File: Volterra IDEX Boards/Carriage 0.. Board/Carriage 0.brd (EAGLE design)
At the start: 84.5 x 61.3 mm, 20 parts, among them K1 FFC/FPC/34PIN/1MMPITCH/TOPLOCK, K2 Tool 0, X1 EXTDR-0, X4 24V, X5 X_LMT

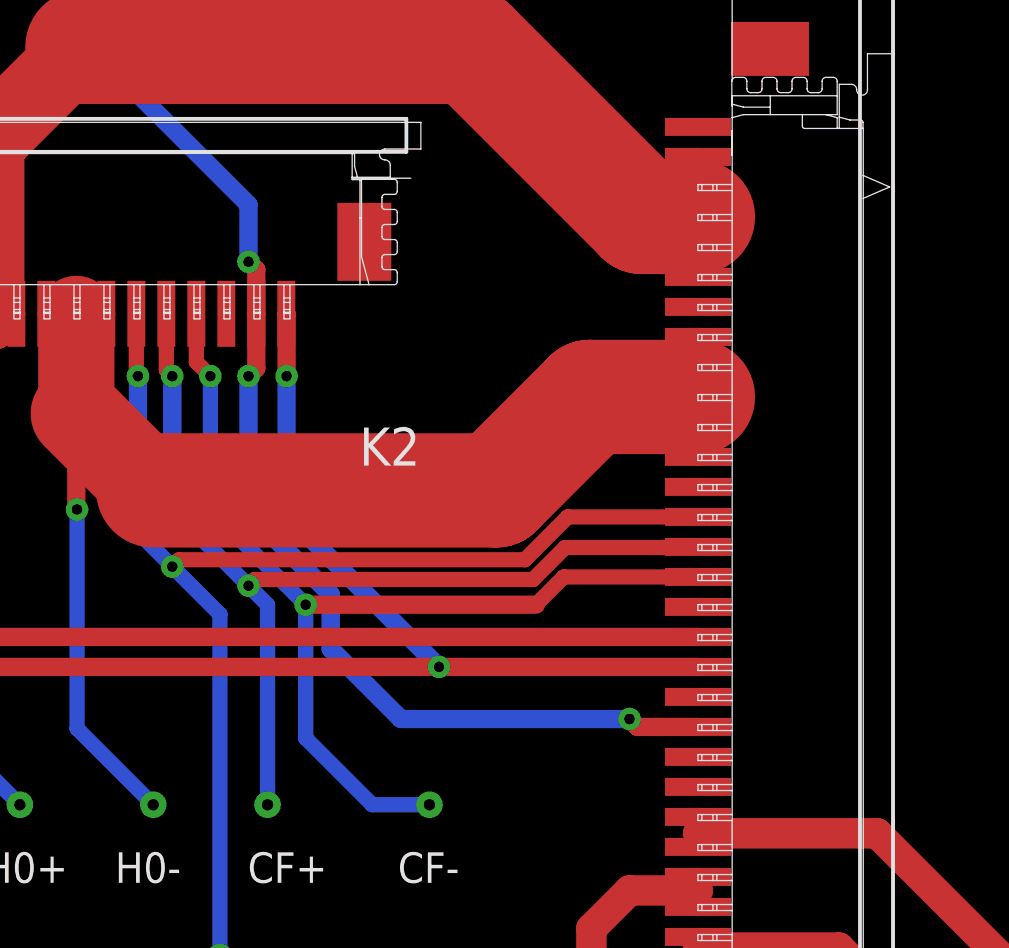
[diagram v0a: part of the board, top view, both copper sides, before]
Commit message: Updated Daughter board schematic and other boards
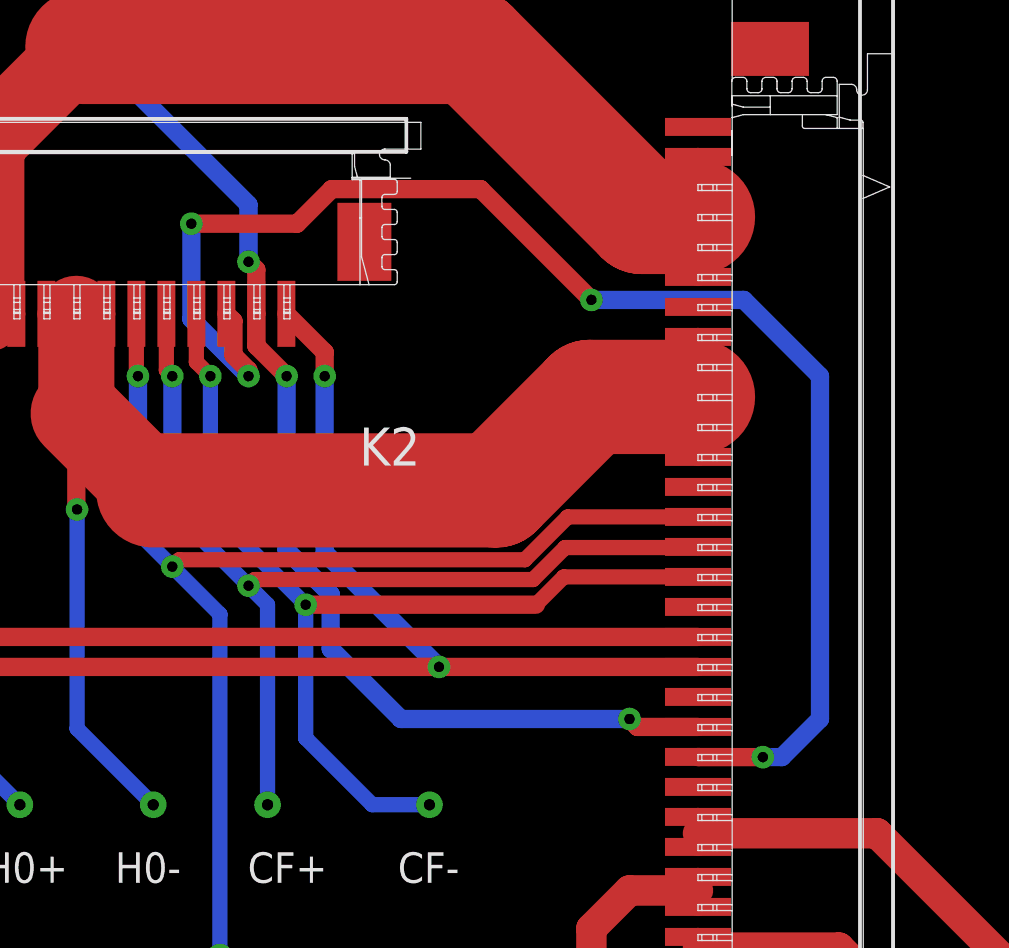
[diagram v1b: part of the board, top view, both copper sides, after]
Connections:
- net 5V: now also K2.3
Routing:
- net 5V: track 0.00 -> 48.3 mm, vias 0 -> 4
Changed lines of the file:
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@@
 </polygon>
 <contactref element="K2" pad="1"/>
-<wire x1="54.601" y1="49.7" x2="54.61" y2="49.691" width="0.6096" layer="1"/>
-<wire x1="54.61" y1="49.691" x2="54.61" y2="47.625" width="0.6096" layer="1"/>
-<via x="54.61" y="47.625" extent="1-16" drill="0.35"/>
-<wire x1="54.61" y1="47.625" x2="54.61" y2="43.011" width="0.6096" layer="16"/>
-<wire x1="54.61" y1="43.011" x2="59.69" y2="37.931" width="0.6096" layer="16"/>
+<wire x1="54.601" y1="49.7" x2="55.88" y2="48.421" width="0.6096" layer="1"/>
+<wire x1="55.88" y1="48.421" x2="55.88" y2="47.625" width="0.6096" layer="1"/>
+<via x="55.88" y="47.625" extent="1-16" drill="0.35"/>
+<wire x1="55.88" y1="47.625" x2="55.88" y2="41.741" width="0.6096" layer="16"/>
+<wire x1="55.88" y1="41.741" x2="59.69" y2="37.931" width="0.6096" layer="16"/>
 <via x="59.69" y="37.931" extent="1-16" drill="0.35"/>
 </signal>
@@
 <wire x1="37.1475" y1="57.15" x2="49.53" y2="57.15" width="0.6096" layer="16"/>
 <wire x1="49.53" y1="57.15" x2="53.34" y2="53.34" width="0.6096" layer="16"/>
-<wire x1="53.601" y1="49.7" x2="53.601" y2="47.886" width="0.6096" layer="1"/>
-<wire x1="53.601" y1="47.886" x2="53.34" y2="47.625" width="0.6096" layer="1"/>
-<via x="53.34" y="47.625" extent="1-16" drill="0.35"/>
-<wire x1="53.34" y1="47.625" x2="53.34" y2="43.0914375" width="0.6096" layer="16"/>
-<wire x1="53.34" y1="43.0914375" x2="56.0804" y2="40.3510375" width="0.6096" layer="16"/>
+<wire x1="53.601" y1="49.7" x2="53.601" y2="48.634" width="0.6096" layer="1"/>
+<wire x1="53.601" y1="48.634" x2="54.61" y2="47.625" width="0.6096" layer="1"/>
+<via x="54.61" y="47.625" extent="1-16" drill="0.35"/>
+<wire x1="54.61" y1="47.625" x2="54.61" y2="41.8214375" width="0.6096" layer="16"/>
+<wire x1="54.61" y1="41.8214375" x2="56.0804" y2="40.3510375" width="0.6096" layer="16"/>
 <wire x1="56.0804" y1="40.3510375" x2="56.0804" y2="38.5346" width="0.6096" layer="16"/>
 <wire x1="58.42" y1="36.195" x2="66.04" y2="36.195" width="0.6096" layer="16"/>
@@
 <signal name="5V">
 <contactref element="K1" pad="13"/>
+<contactref element="K2" pad="3"/>
+<via x="53.34" y="47.625" extent="1-16" drill="0.35"/>
+<wire x1="52.601" y1="49.7" x2="52.839" y2="49.462" width="0.6096" layer="1"/>
+<wire x1="53.34" y1="47.81736875" x2="53.34" y2="47.625" width="0.6096" layer="1"/>
+<wire x1="52.839" y1="49.462" x2="52.839" y2="48.31836875" width="0.6096" layer="1"/>
+<wire x1="52.839" y1="48.31836875" x2="53.34" y2="47.81736875" width="0.6096" layer="1"/>
+<wire x1="53.34" y1="47.625" x2="51.435" y2="49.53" width="0.6096" layer="16"/>
+<wire x1="51.435" y1="49.53" x2="51.435" y2="52.705" width="0.6096" layer="16"/>
+<via x="51.435" y="52.705" extent="1-16" drill="0.35"/>
+<via x="64.77" y="50.165" extent="1-16" drill="0.35"/>
+<wire x1="51.435" y1="52.705" x2="54.95941875" y2="52.705" width="0.6096" layer="1"/>
+<wire x1="54.95941875" y1="52.705" x2="56.11161875" y2="53.8572" width="0.6096" layer="1"/>
+<wire x1="56.11161875" y1="53.8572" x2="61.0778" y2="53.8572" width="0.6096" layer="1"/>
+<wire x1="61.0778" y1="53.8572" x2="64.77" y2="50.165" width="0.6096" layer="1"/>
+<wire x1="64.77" y1="50.165" x2="69.85" y2="50.165" width="0.6096" layer="16"/>
+<wire x1="69.85" y1="50.165" x2="72.39" y2="47.625" width="0.6096" layer="16"/>
+<wire x1="72.39" y1="47.625" x2="72.39" y2="36.195" width="0.6096" layer="16"/>
+<wire x1="71.12" y1="34.925" x2="70.485" y2="34.925" width="0.6096" layer="16"/>
+<via x="70.485" y="34.925" extent="1-16" drill="0.35"/>
+<wire x1="70.485" y1="34.925" x2="68.329" y2="34.925" width="0.6096" layer="1"/>
+<wire x1="68.329" y1="34.925" x2="68.323" y2="34.931" width="0.6096" layer="1"/>
+<wire x1="72.39" y1="36.195" x2="71.12" y2="34.925" width="0.6096" layer="16"/>
 </signal>
 <signal name="CF+1">

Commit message: DRC checked of Chassis, Carriage 1 & 2, and created CAM files
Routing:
- net B0+: track 48.9 -> 41.8 mm
- net 5V: track 48.3 -> 49.2 mm
- net CF+: track 33.3 -> 34.0 mm
- net H0-: track 46.5 -> 46.0 mm
- net PT0: track 40.8 -> 41.3 mm

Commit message: Board files added
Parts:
- moved TP1 0.61 mm to (35.7, 56.5), flipped to the bottom
- moved TP10 0.16 mm to (37.2, 23.0), flipped to the bottom
- moved X4 0.12 mm to (34.3, 48.5), flipped to the top
- flipped TP11 to the bottom
- flipped TP12 to the bottom
- flipped TP13 to the bottom
- flipped TP3 to the bottom
- flipped TP4 to the bottom
- flipped TP5 to the bottom
- flipped TP6 to the bottom
- flipped TP7 to the bottom
- flipped TP8 to the bottom
- flipped TP9 to the bottom
- flipped X5 to the top
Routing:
- net 24V: track 56.3 -> 68.3 mm, vias 3 -> 4
- net X0_LMT: track 56.5 -> 46.7 mm, vias 1 -> 2
- net GND: track 82.7 -> 75.5 mm, vias 2 -> 3
- net B0-: track 58.0 -> 58.2 mm, vias 0 -> 1
- net A0+: track 49.8 -> 49.7 mm, vias 0 -> 1
- net PT0: track 41.3 -> 41.4 mm, vias 2 -> 3
- net H0-: vias 1 -> 2
- net H0+: vias 1 -> 2
- net CF-: vias 2 -> 3
- net CF+: vias 2 -> 3
- net B0+: vias 0 -> 1
- net A0-: vias 0 -> 1
